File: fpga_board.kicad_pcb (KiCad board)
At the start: 8 copper layers, 50 x 50 mm, 10 parts, among them U1 LFE5U-45F-7BG256I, U10 TLV62569DRL, U2 CYUSB3014-BZXC, U3 K4B4G1646E-BCMA, U4 K4B4G1646E-BCMA, U5 K4B4G1646E-BCMA, U6 K4B4G1646E-BCMA, U7 TLV62569DRL, U8 TLV62569DRL, U9 TLV62569DRL

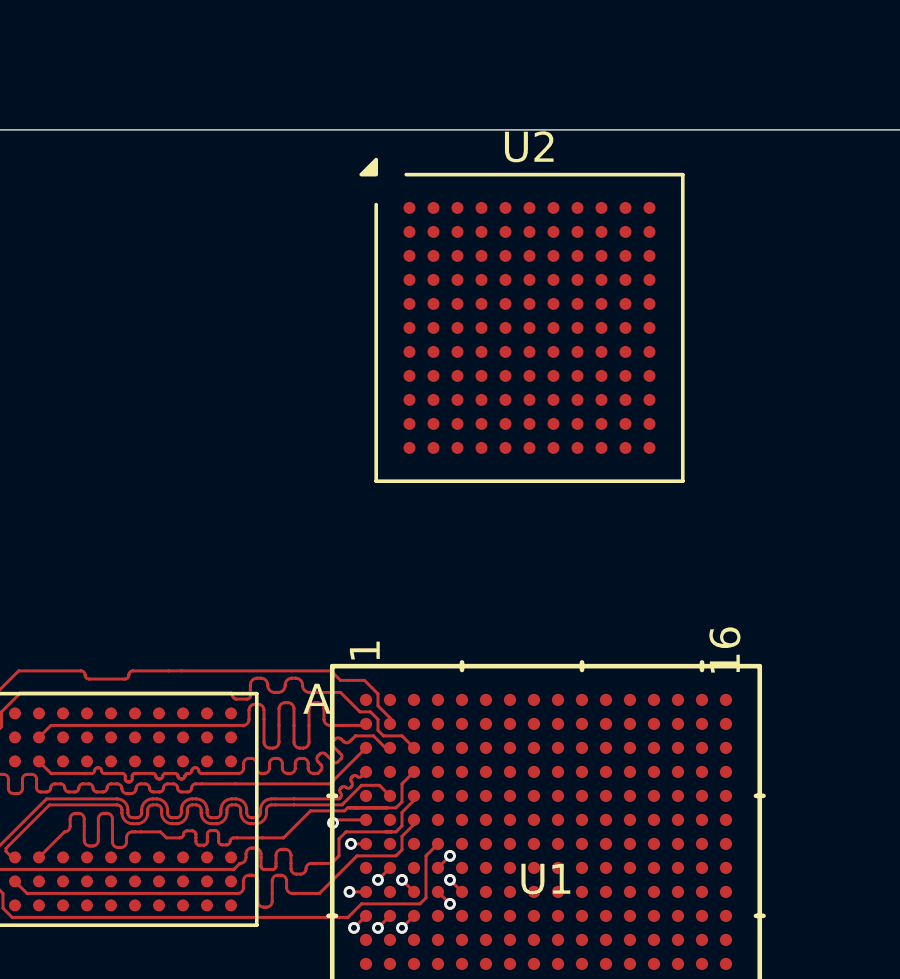
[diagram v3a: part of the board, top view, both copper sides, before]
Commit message: layer 3 FX3 length matched
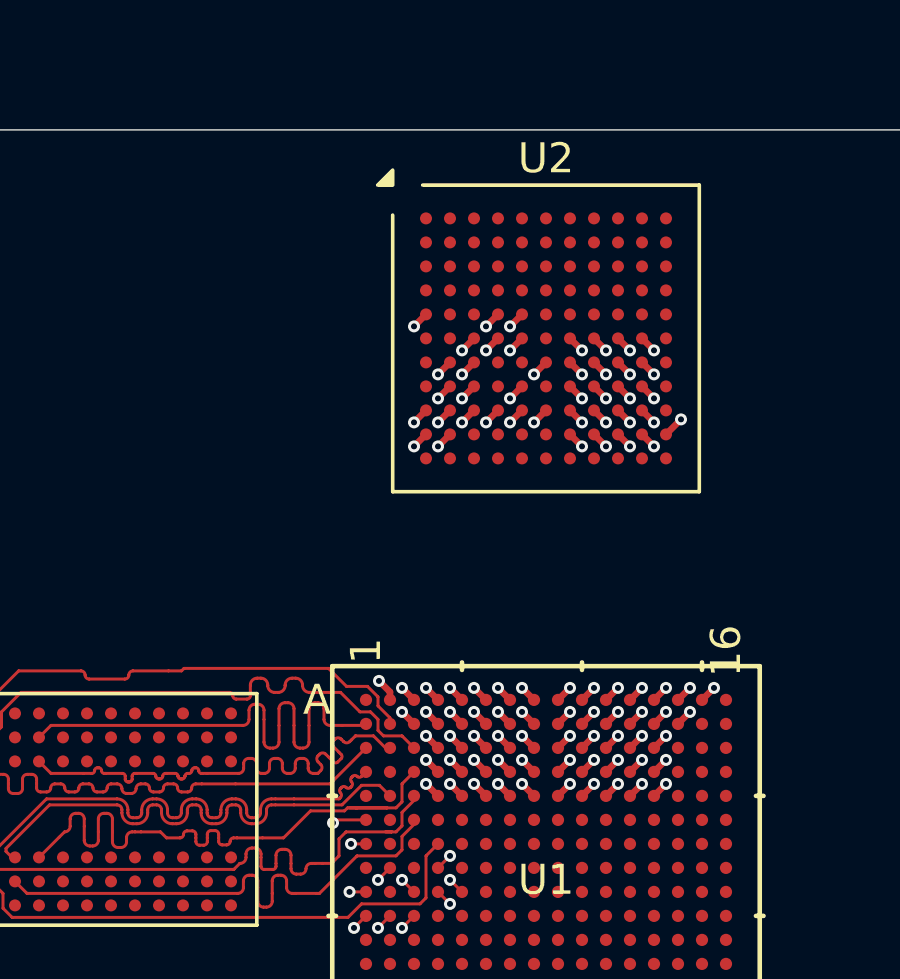
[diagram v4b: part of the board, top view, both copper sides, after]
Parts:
- moved U2 0.65 mm to (95.0, 47.0)
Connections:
- U1 pad A10: unconnected-(U1C-PT51B-PadA10) -> FIFO.SLCS#
- U1 pad A11: unconnected-(U1C-PT71A-PadA11) -> FIFO_DQ14
- U1 pad A12: unconnected-(U1C-PT71B-PadA12) -> FIFO_DQ9
- U1 pad A13: unconnected-(U1C-PT83A-PadA13) -> FIFO_DQ8
- U1 pad A14: unconnected-(U1C-PT83B-PadA14) -> FIFO_DQ6
- U1 pad A15: unconnected-(U1C-PT85B-PadA15) -> FIFO_DQ0
- U1 pad A2: unconnected-(U1B-PT4A-PadA2) -> FIFO_DQ22
- U1 pad A3: unconnected-(U1B-PT6A-PadA3) -> FIFO_DQ18
- U1 pad A4: unconnected-(U1B-PT6B-PadA4) -> FIFO_DQ19
- U1 pad A5: unconnected-(U1C-PT18A-PadA5) -> FIFO_DQ20
- U1 pad A6: unconnected-(U1C-PT18B-PadA6) -> FIFO_DQ17
- U1 pad A7: unconnected-(U1C-PT38A-PadA7) -> FIFO.A1
- U1 pad A8: unconnected-(U1C-PT38B-PadA8) -> FIFO.CLK
- U1 pad A9: unconnected-(U1C-PT51A-PadA9) -> FIFO.SLWR#
- U1 pad B10: unconnected-(U1C-PT53A-PadB10) -> FIFO.PKTEND#
- U1 pad B11: unconnected-(U1C-PT58A-PadB11) -> FIFO_DQ13
- U1 pad B12: unconnected-(U1C-PT74A-PadB12) -> FIFO_DQ12
- U1 pad B13: unconnected-(U1C-PT78A-PadB13) -> FIFO_DQ10
- U1 pad B14: unconnected-(U1C-PT85A-PadB14) -> FIFO_DQ3
- U1 pad B3: unconnected-(U1B-PT4B-PadB3) -> FIFO_DQ21
- U1 pad B4: unconnected-(U1B-PT11B-PadB4) -> FIFO_DQ16
- U1 pad B5: unconnected-(U1C-PT15B-PadB5) -> FIFO_DQ28
- U1 pad B6: unconnected-(U1C-PT31B-PadB6) -> FIFO.A0
- U1 pad B7: unconnected-(U1C-PT36B-PadB7) -> FIFO_DQ24
- U1 pad B8: unconnected-(U1C-PT44B-PadB8) -> FIFO.FLAG_B
- U1 pad B9: unconnected-(U1C-PT47A-PadB9) -> FIFO.SLOE#
- U1 pad C10: unconnected-(U1C-PT53B-PadC10) -> FIFO.FLAG_A
- U1 pad C11: unconnected-(U1C-PT58B-PadC11) -> FIFO_DQ15
- U1 pad C12: unconnected-(U1C-PT74B-PadC12) -> FIFO_DQ7
- U1 pad C13: unconnected-(U1C-PT78B-PadC13) -> FIFO_DQ4
- U1 pad C4: unconnected-(U1B-PT11A-PadC4) -> FIFO_DQ25
- U1 pad C5: unconnected-(U1C-PT15A-PadC5) -> FIFO_DQ26
- U1 pad C6: unconnected-(U1C-PT31A-PadC6) -> FIFO_DQ23
- U1 pad C7: unconnected-(U1C-PT36A-PadC7) -> FIFO_DQ31
- U1 pad C8: unconnected-(U1C-PT44A-PadC8) -> FIFO_DQ30
- U1 pad C9: unconnected-(U1C-PT47B-PadC9) -> FIFO.SLRD#
- U1 pad D12: unconnected-(U1C-PT76A-PadD12) -> FIFO_DQ1
- U1 pad D13: unconnected-(U1C-PT80A-PadD13) -> FIFO_DQ5
- U1 pad D4: unconnected-(U1B-PT9B-PadD4) -> FIFO_DQ29
- U1 pad D5: unconnected-(U1B-PT13B-PadD5) -> FIFO_DQ27
- U1 pad D9: unconnected-(U1C-PT49A-PadD9) -> FIFO_DQ2
- U1 pad F10: Net-(U1D-VCCIO1-PadF10) -> 3v3
- U1 pad F11: Net-(U1D-VCCIO1-PadF10) -> 3v3
- U1 pad F6: Net-(U1D-VCCIO0-PadF6) -> 3v3
- U1 pad F7: Net-(U1D-VCCIO0-PadF6) -> 3v3
- U2 pad G7: FIFO.FLAGA -> FIFO.FLAG_A
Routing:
- net FIFO.SLCS#: track 0.00 -> 20.0 mm, vias 0 -> 2
- net FIFO_DQ3: track 0.00 -> 19.1 mm, vias 0 -> 2
- net FIFO_DQ22: track 0.00 -> 19.1 mm, vias 0 -> 2
- net FIFO_DQ5: track 0.00 -> 19.1 mm, vias 0 -> 2
- net FIFO_DQ0: track 0.00 -> 19.0 mm, vias 0 -> 2
- net FIFO_DQ21: track 0.00 -> 19.0 mm, vias 0 -> 2
- net FIFO_DQ6: track 0.00 -> 19.0 mm, vias 0 -> 2
- net FIFO_DQ18: track 0.00 -> 19.0 mm, vias 0 -> 2
- net FIFO_DQ10: track 0.00 -> 19.0 mm, vias 0 -> 2
- net FIFO_DQ8: track 0.00 -> 19.0 mm, vias 0 -> 2
- net FIFO_DQ12: track 0.00 -> 19.0 mm, vias 0 -> 2
- net FIFO.A1: track 0.00 -> 19.0 mm, vias 0 -> 2
- net FIFO_DQ14: track 0.00 -> 19.0 mm, vias 0 -> 2
- net FIFO.PKTEND#: track 0.00 -> 19.0 mm, vias 0 -> 2
- net FIFO_DQ9: track 0.00 -> 18.9 mm, vias 0 -> 2
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
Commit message: minor changes
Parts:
- moved U3 18.2 mm to (111.3, 62.0), turned to -90 degrees
- moved U4 8.88 mm to (111.3, 71.8), turned to -90 degrees
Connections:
- net SPI_MISO renamed SPI.MISO
- net SPI_MOSI renamed SPI.MOSI
- net SPI_SCK renamed SPI.SCK
- net SPI_SSN renamed SPI.SSN
- U1 pad D12: FIFO_DQ1 -> FIFO_DQ5
- U1 pad D13: FIFO_DQ5 -> FIFO_DQ1
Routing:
- net FIFO.FLAG_A: track 13.9 -> 20.4 mm
- net FIFO_DQ7: track 12.9 -> 17.8 mm
- net FIFO.SLRD#: track 12.8 -> 17.7 mm
- net FIFO_DQ23: track 12.9 -> 17.6 mm
- net FIFO_DQ24: track 13.7 -> 17.7 mm
- net FIFO_DQ15: track 13.7 -> 17.7 mm
- net FIFO_DQ25: track 14.0 -> 17.7 mm
- net FIFO_DQ26: track 14.2 -> 17.7 mm
- net FIFO_DQ4: track 14.6 -> 17.7 mm
- net FIFO_DQ30: track 15.3 -> 17.8 mm
- net FIFO_DQ31: track 15.3 -> 17.8 mm
- net FIFO_DQ2: track 15.5 -> 17.8 mm
- net FIFO_DQ5: track 19.1 -> 17.8 mm
- net FIFO_DQ29: track 17.1 -> 17.8 mm
- net FIFO_DQ27: track 17.2 -> 17.9 mm
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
